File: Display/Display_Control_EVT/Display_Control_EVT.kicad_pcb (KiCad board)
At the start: 2 copper layers, 81.3 x 40.6 mm, 4 parts, among them J1 Conn_01x60, J2 Conn_01x60_Pin

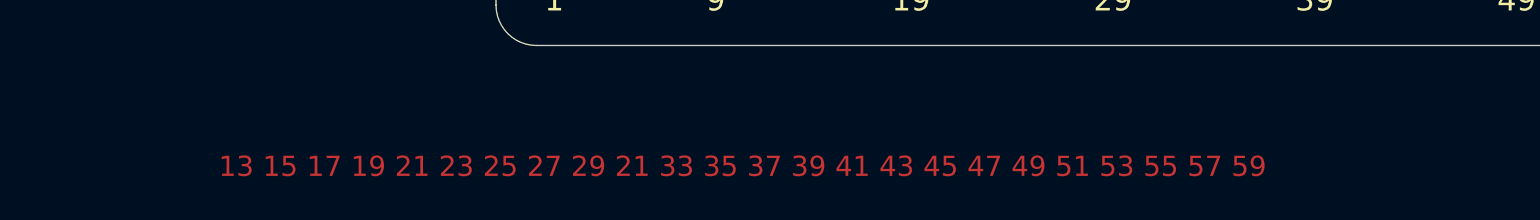
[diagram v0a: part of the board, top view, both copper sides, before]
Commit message: remove unused top label
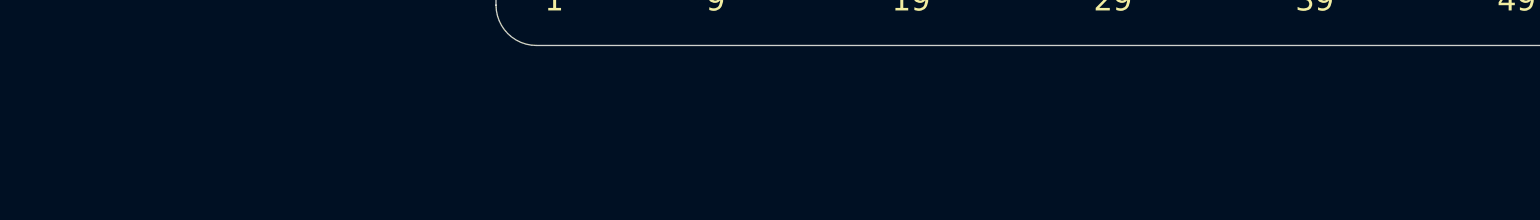
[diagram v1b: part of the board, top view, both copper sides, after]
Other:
- board text removed: "13 15 17 19 21 23 25 27 29 21 33 35 37 39 41 43 45 47 49 51 53 55 57 59"
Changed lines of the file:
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@@
 		(layer "Edge.Cuts")
-	)
-	(gr_text " 13 15 17 19 21 23 25 27 29 21 33 35 37 39 41 43 45 47 49 51 53 55 57 59"
-		(at 101.6 142.24 0)
-		(layer "F.Cu")
-		(effects
-			(font
-				(size 1.27 1.27)
-			)
-		)
 	)
 	(gr_text "9"
